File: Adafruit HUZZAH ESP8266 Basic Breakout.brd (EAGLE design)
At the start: 25.4 x 38.1 mm, 30 parts, among them SW1 KMR2, SW2 KMR2, U1 SPX3819, X1 ESP-12

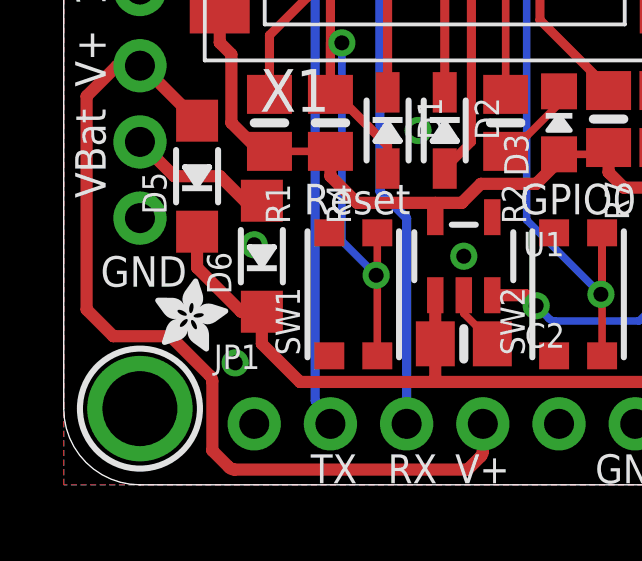
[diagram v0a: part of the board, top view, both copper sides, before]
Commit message: Modified board to have VHS (hackspace.ca) logo
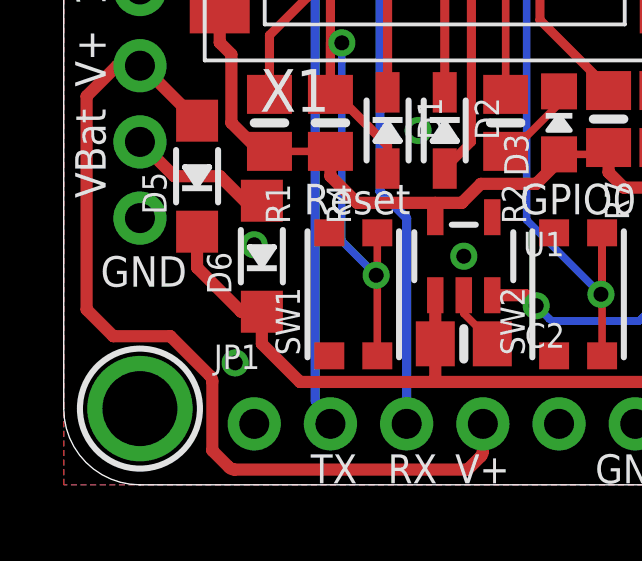
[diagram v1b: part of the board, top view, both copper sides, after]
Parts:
- removed U$12: (no value), microbuilder:ADAFRUIT_TEXT_20MM
- removed U$13: (no value), microbuilder:PCBFEAT-REV-040
- removed U$3: (no value), microbuilder:ADAFRUIT_2.5MM
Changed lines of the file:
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@@
 <?xml version="1.0" encoding="utf-8"?>
 <!DOCTYPE eagle SYSTEM "eagle.dtd">
-<eagle version="6.6.0">
+<eagle version="6.5.0">
 <drawing>
 <settings>
@@
 <setting verticaltext="up"/>
 </settings>
-<grid distance="0.005" unitdist="inch" unit="inch" style="lines" multiple="1" display="no" altdistance="0.025" altunitdist="inch" altunit="inch"/>
+<grid distance="0.005" unitdist="inch" unit="mm" style="lines" multiple="1" display="no" altdistance="0.025" altunitdist="inch" altunit="inch"/>
 <layers>
 <layer number="1" name="Top" color="4" fill="1" visible="yes" active="yes"/>
@@
 <text x="10.414" y="11.684" size="1.016" layer="22" font="vector" ratio="12" rot="MR0" align="center">Contains FCC ID
 2ADUIESP-12</text>
+<polygon width="0" layer="22">
+<vertex x="15.2841" y="8.6116"/>
+<vertex x="16.2197" y="4.55265"/>
+<vertex x="16.11225" y="4.22495"/>
+<vertex x="17.094" y="4.22495"/>
+<vertex x="18.2903" y="8.6116"/>
+<vertex x="17.3365" y="8.61245"/>
+<vertex x="16.43025" y="5.34695"/>
+<vertex x="15.67775" y="8.61055"/>
+</polygon>
+<polygon width="0" layer="22">
+<vertex x="12.83025" y="5.8507"/>
+<vertex x="13.1674" y="5.48255"/>
+<vertex x="13.96495" y="5.48255"/>
+<vertex x="13.96495" y="4.22495"/>
+<vertex x="14.8853" y="4.22495"/>
+<vertex x="14.8853" y="5.48255"/>
+<vertex x="15.2339" y="5.48255"/>
+<vertex x="14.8853" y="5.8507"/>
+<vertex x="14.8853" y="8.6116"/>
+<vertex x="13.96495" y="8.6116"/>
+<vertex x="13.96495" y="5.8507"/>
+</polygon>
+<polygon width="0" layer="22">
+<vertex x="11.90955" y="4.22495"/>
+<vertex x="12.82995" y="4.22495"/>
+<vertex x="12.82995" y="8.6116"/>
+<vertex x="11.90955" y="8.6116"/>
+</polygon>
+<polygon width="0" layer="22">
+<vertex x="8.30495" y="5.45355"/>
+<vertex x="8.3326" y="5.1779"/>
+<vertex x="8.4156" y="4.93515"/>
+<vertex x="8.554" y="4.72495"/>
+<vertex x="8.7474" y="4.5472"/>
+<vertex x="9.19765" y="4.30555"/>
+<vertex x="9.6624" y="4.22495"/>
+<vertex x="11.10035" y="4.22495"/>
+<vertex x="11.23105" y="4.59305"/>
+<vertex x="9.9876" y="4.59305"/>
+<vertex x="9.5924" y="4.6373"/>
+<vertex x="9.3357" y="4.7691"/>
+<vertex x="9.1955" y="4.95685"/>
+<vertex x="9.14855" y="5.1671"/>
+<vertex x="9.16405" y="5.37485"/>
+<vertex x="9.20935" y="5.5146"/>
+<vertex x="9.3206" y="5.62445"/>
+<vertex x="9.5324" y="5.7413"/>
+<vertex x="10.6842" y="6.1241"/>
+<vertex x="11.00025" y="6.2839"/>
+<vertex x="11.28015" y="6.52155"/>
+<vertex x="11.4774" y="6.87035"/>
+<vertex x="11.5428" y="7.3627"/>
+<vertex x="11.51425" y="7.6432"/>
+<vertex x="11.428" y="7.89035"/>
+<vertex x="11.28455" y="8.1041"/>
+<vertex x="11.0835" y="8.28445"/>
+<vertex x="10.5874" y="8.53"/>
+<vertex x="10.018" y="8.6116"/>
+<vertex x="8.3817" y="8.6116"/>
+<vertex x="8.4829" y="8.24355"/>
+<vertex x="9.4337" y="8.24355"/>
+<vertex x="9.89675" y="8.20585"/>
+<vertex x="10.29355" y="8.09245"/>
+<vertex x="10.4531" y="8.00265"/>
+<vertex x="10.56675" y="7.88355"/>
+<vertex x="10.6351" y="7.7354"/>
+<vertex x="10.65765" y="7.55855"/>
+<vertex x="10.6346" y="7.38905"/>
+<vertex x="10.5649" y="7.2428"/>
+<vertex x="10.4488" y="7.11965"/>
+<vertex x="10.2857" y="7.01985"/>
+<vertex x="9.88755" y="6.8614"/>
+<vertex x="9.43615" y="6.7377"/>
+<vertex x="8.9964" y="6.58445"/>
+<vertex x="8.63185" y="6.33485"/>
+<vertex x="8.48885" y="6.1686"/>
+<vertex x="8.38685" y="5.96625"/>
+<vertex x="8.3256" y="5.7278"/>
+</polygon>
 </plain>
 <attributes>
@@
 </element>
 <element name="U$2" library="microbuilder" package="HUZZAHLOGO" value="" x="21.59" y="30.607" rot="MR0"/>
-<element name="U$12" library="microbuilder" package="ADAFRUIT_TEXT_20MM" value="" x="22.606" y="4.699" rot="MR0"/>
-<element name="U$13" library="microbuilder" package="PCBFEAT-REV-040" value="" x="20.066" y="5.08" rot="MR0"/>
 <element name="D3" library="microbuilder" package="CHIPLED_0805_NOOUTLINE" value="RED" x="16.51" y="12.065" smashed="yes">
 <attribute name="NAME" x="15.494" y="10.287" size="0.8128" layer="25" ratio="18" rot="R90"/>
@@
 <attribute name="VALUE" x="15.113" y="14.351" size="0.8128" layer="27" ratio="10" rot="R90"/>
 </element>
-<element name="U$3" library="microbuilder" package="ADAFRUIT_2.5MM" value="" x="3.048" y="4.445" smashed="yes"/>
 </elements>
 <signals>
